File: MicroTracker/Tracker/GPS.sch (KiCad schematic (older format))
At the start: 2 parts, among them U2 TESEO-LIV3F, U3 GP.1575.15.4.B.02

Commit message: started working on gps
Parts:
- removed U2: TESEO-LIV3F, LCC18_9P7X10P1_STM, symbol MicroTracker:TESEO-LIV3F
- removed U3: GP.1575.15.4.B.02, GP.1575.15.4.B.02_TAL, symbol MicroTracker:GP.1575.15.4.B.02
- added BT?: Battery_Cell, symbol Device:Battery_Cell
- added C?: 120pF, symbol Device:C
- added C?: 120p, symbol Device:C
- added C?: 56p, symbol Device:C
- added C?: 1u, symbol Device:C
- added C?: 2.2u, symbol Device:C
- added C?: 100p, symbol Device:C
- added C?: 100n, symbol Device:C
- added C?: 1n, symbol Device:C
- added D?: D_TVS_ALT, symbol Device:D_TVS_ALT
- added F?: B4327, symbol local-symbols:B4327
- added L?: 6.8n, symbol Device:L
- added L?: 56n, symbol Device:L
- added R? (x4): 0, symbol Device:R
- added R?: R, symbol Device:R
- added R?: 100k, symbol Device:R
- added R?: 10k, symbol Device:R
- added U?: TESEO-LIV3F, symbol local-symbols:TESEO-LIV3F
- added U?: BGA725L6, symbol local-symbols:BGA725L6
- added U?: GP.1575.15.4.B.02, GP.1575.15.4.B.02_TAL, symbol MicroTracker:GP.1575.15.4.B.02
- added U?: TPS22943, symbol local-symbols:TPS22943
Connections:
- net labels added: +3.3V, +BATT, ANT_OFF, RF_IN, VCC_RF
- wire segments 5 -> 75
- no-connect marks 2 -> 0
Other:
- note removed: "GPS\n"

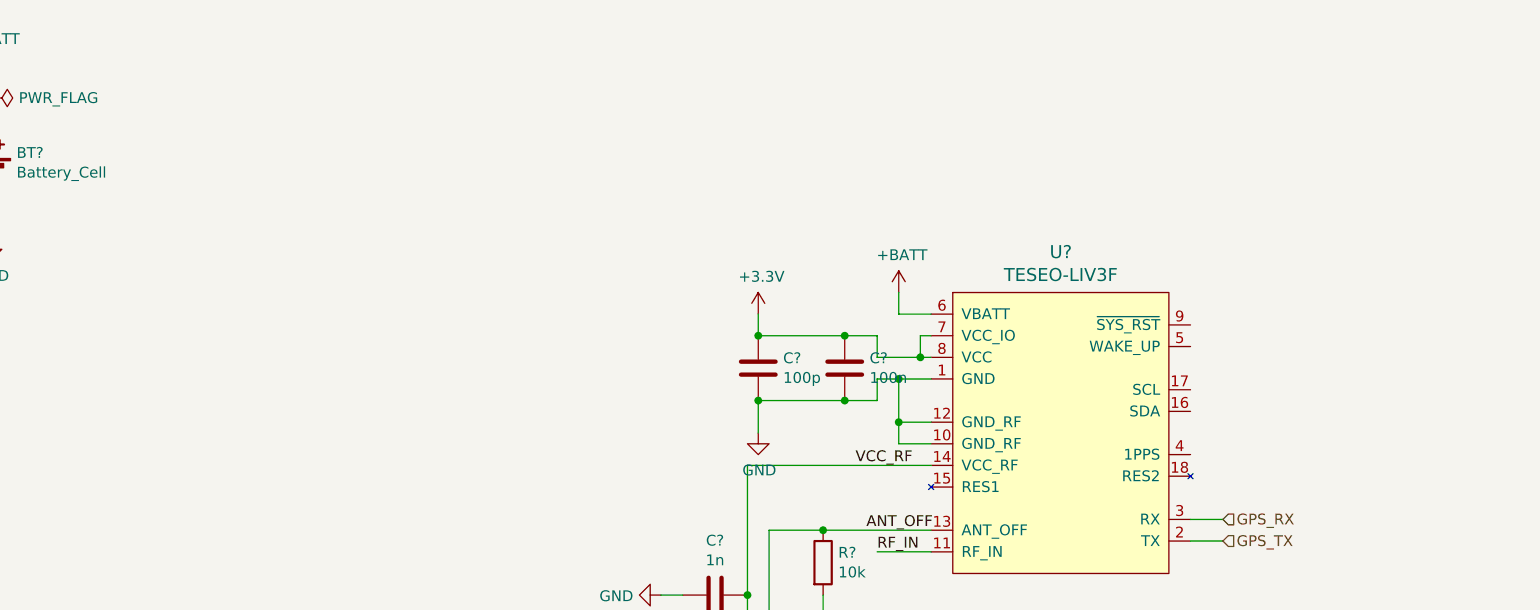
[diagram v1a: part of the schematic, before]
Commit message: gps finished
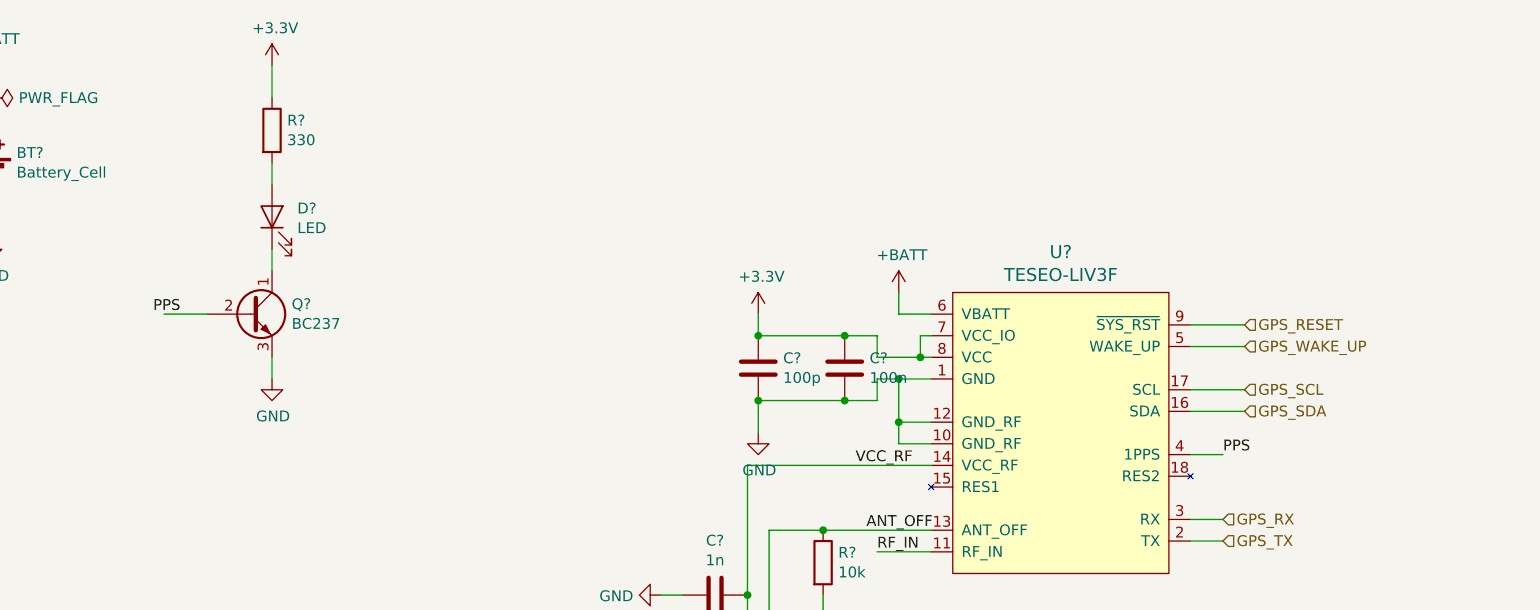
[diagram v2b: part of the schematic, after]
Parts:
- added D?: LED, symbol Device:LED
- added Q?: BC237, Package_TO_SOT_THT:TO-92_Inline, symbol Transistor_BJT:BC237
- added R?: 330, symbol Device:R
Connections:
- net +3V3: now also R?.1
- net GND: now also Q?.3 (E)
- net GPS_SDA: now reaches U?.16 (SDA)
- net GPS_SCL: now reaches U?.17 (SCL)
- net PPS: now reaches U?.4 (1PPS)
- net GPS_WAKE_UP: now reaches U?.5 (WAKE_UP)
- net GPS_RESET: now reaches U?.9 (~SYS_RST)
- new net: D?.2 (A), R?.2
- new net: D?.1 (K), Q?.1 (C)
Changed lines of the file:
@@
 Wire Wire Line
 	4800 3500 4900 3500
+Text Label 7400 2850 0    50   ~ 0
+PPS
+Wire Wire Line
+	7250 2850 7400 2850
+$Comp
+L power:+3.3V #PWR?
+U 1 1 5F0DD0CB
+P 3000 1050
+F 0 "#PWR?" H 3000 900 50  0001 C CNN
+F 1 "+3.3V" H 3015 1223 50  0000 C CNN
+F 2 "" H 3000 1050 50  0001 C CNN
+F 3 "" H 3000 1050 50  0001 C CNN
+	1    3000 1050
+	1    0    0    -1
+$EndComp
+$Comp
+L Device:R R?
+U 1 1 5F0DDA09
+P 3000 1350
+F 0 "R?" H 3070 1396 50  0000 L CNN
+F 1 "330" H 3070 1305 50  0000 L CNN
+F 2 "" V 2930 1350 50  0001 C CNN
+F 3 "~" H 3000 1350 50  0001 C CNN
+	1    3000 1350
+	1    0    0    -1
+$EndComp
+$Comp
+L Device:LED D?
+U 1 1 5F0DE437
+P 3000 1750
+F 0 "D?" V 3039 1633 50  0000 R CNN
+F 1 "LED" V 2948 1633 50  0000 R CNN
+F 2 "" H 3000 1750 50  0001 C CNN
+F 3 "~" H 3000 1750 50  0001 C CNN
+	1    3000 1750
+	0    -1   -1   0
+$EndComp
+$Comp
+L power:GND #PWR?
+U 1 1 5F0DF596
+P 3000 2500
+F 0 "#PWR?" H 3000 2250 50  0001 C CNN
+F 1 "GND" H 3005 2327 50  0000 C CNN
+F 2 "" H 3000 2500 50  0001 C CNN
+F 3 "" H 3000 2500 50  0001 C CNN
+	1    3000 2500
+	1    0    0    -1
+$EndComp
+Wire Wire Line
+	3000 1050 3000 1200
+Wire Wire Line
+	3000 1500 3000 1600
+$Comp
+L Transistor_BJT:BC237 Q?
+U 1 1 5F0E52E0
+P 2900 2200
+F 0 "Q?" H 3091 2246 50  0000 L CNN
+F 1 "BC237" H 3091 2155 50  0000 L CNN
+F 2 "Package_TO_SOT_THT:TO-92_Inline" H 3100 2125 50  0001 L CIN
+F 3 "http://www.onsemi.com/pub_link/Collateral/BC237-D.PDF" H 2900 2200 50  0001 L CNN
+	1    2900 2200
+	1    0    0    -1
+$EndComp
+Text Label 2450 2200 0    50   ~ 0
+PPS
+Wire Wire Line
+	3000 1900 3000 2000
+Wire Wire Line
+	2500 2200 2700 2200
+Wire Wire Line
+	3000 2400 3000 2500
+Text HLabel 7500 2250 2    50   Input ~ 0
+GPS_RESET
+Text HLabel 7500 2350 2    50   Input ~ 0
+GPS_WAKE_UP
+Text HLabel 7500 2550 2    50   Input ~ 0
+GPS_SCL
+Text HLabel 7500 2650 2    50   Input ~ 0
+GPS_SDA
+Wire Wire Line
+	7250 2250 7500 2250
+Wire Wire Line
+	7250 2350 7500 2350
+Wire Wire Line
+	7250 2550 7500 2550
+Wire Wire Line
+	7250 2650 7500 2650
 $EndSCHEMATC

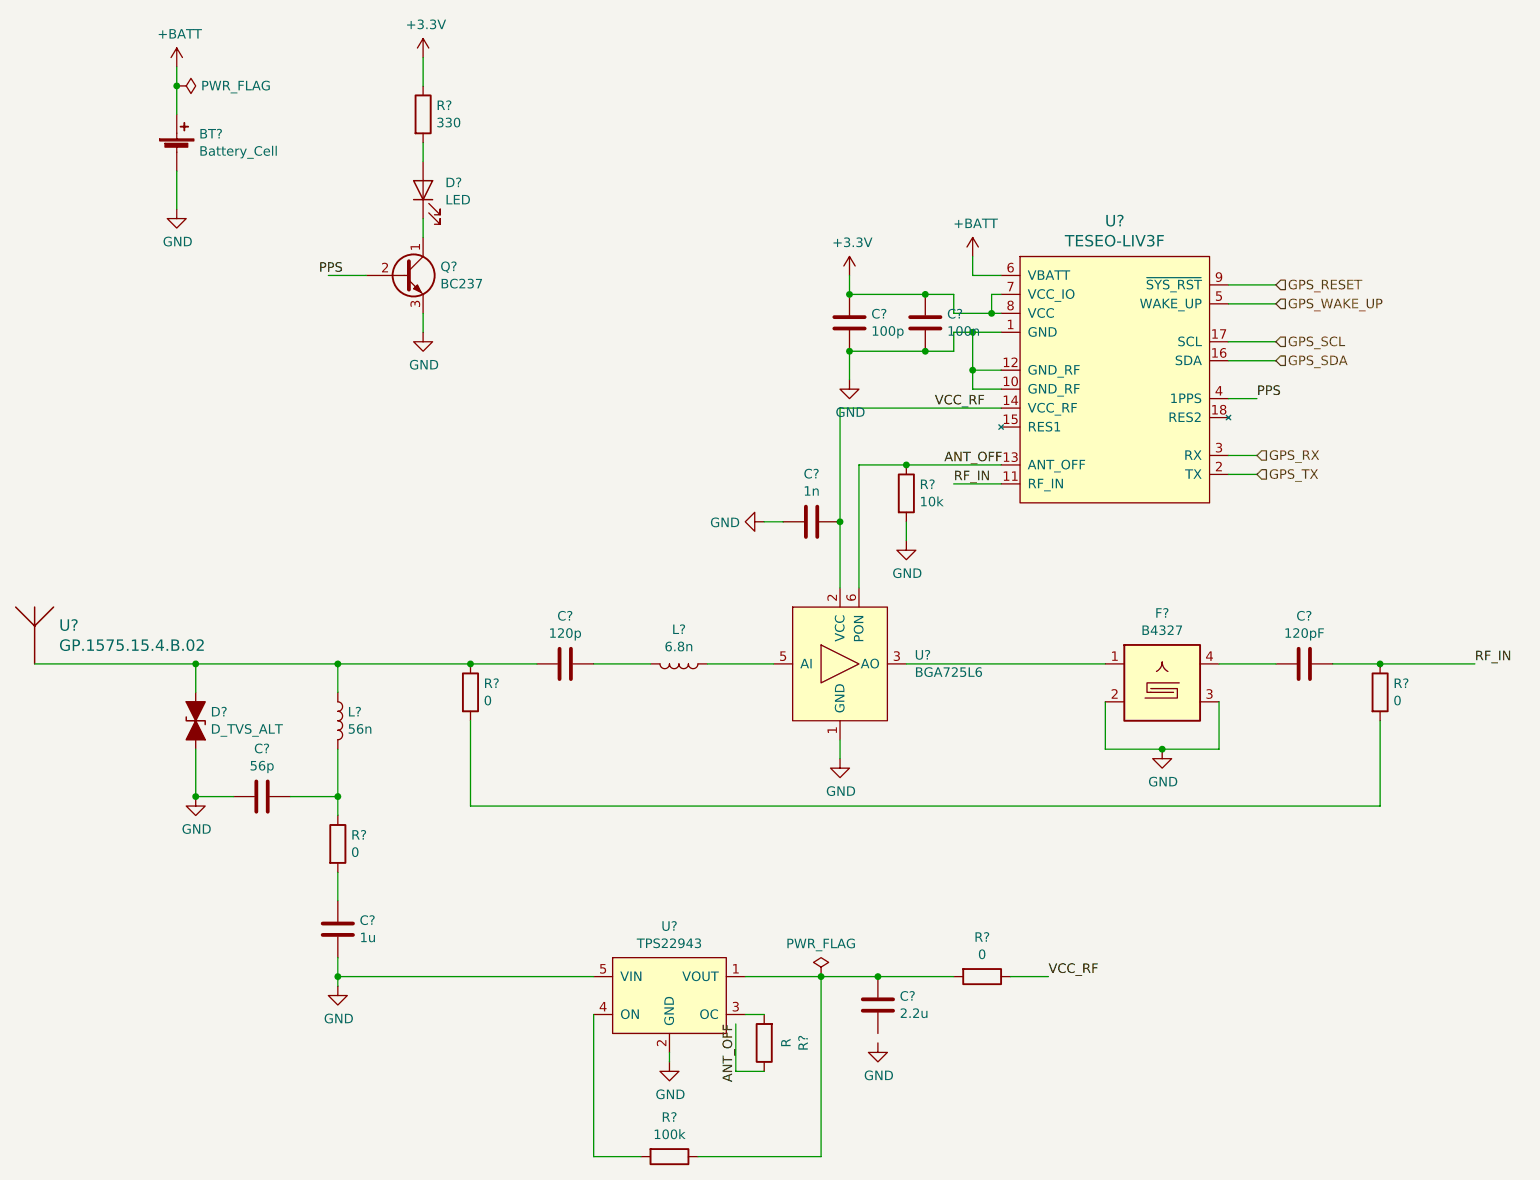
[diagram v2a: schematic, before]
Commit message: added charges
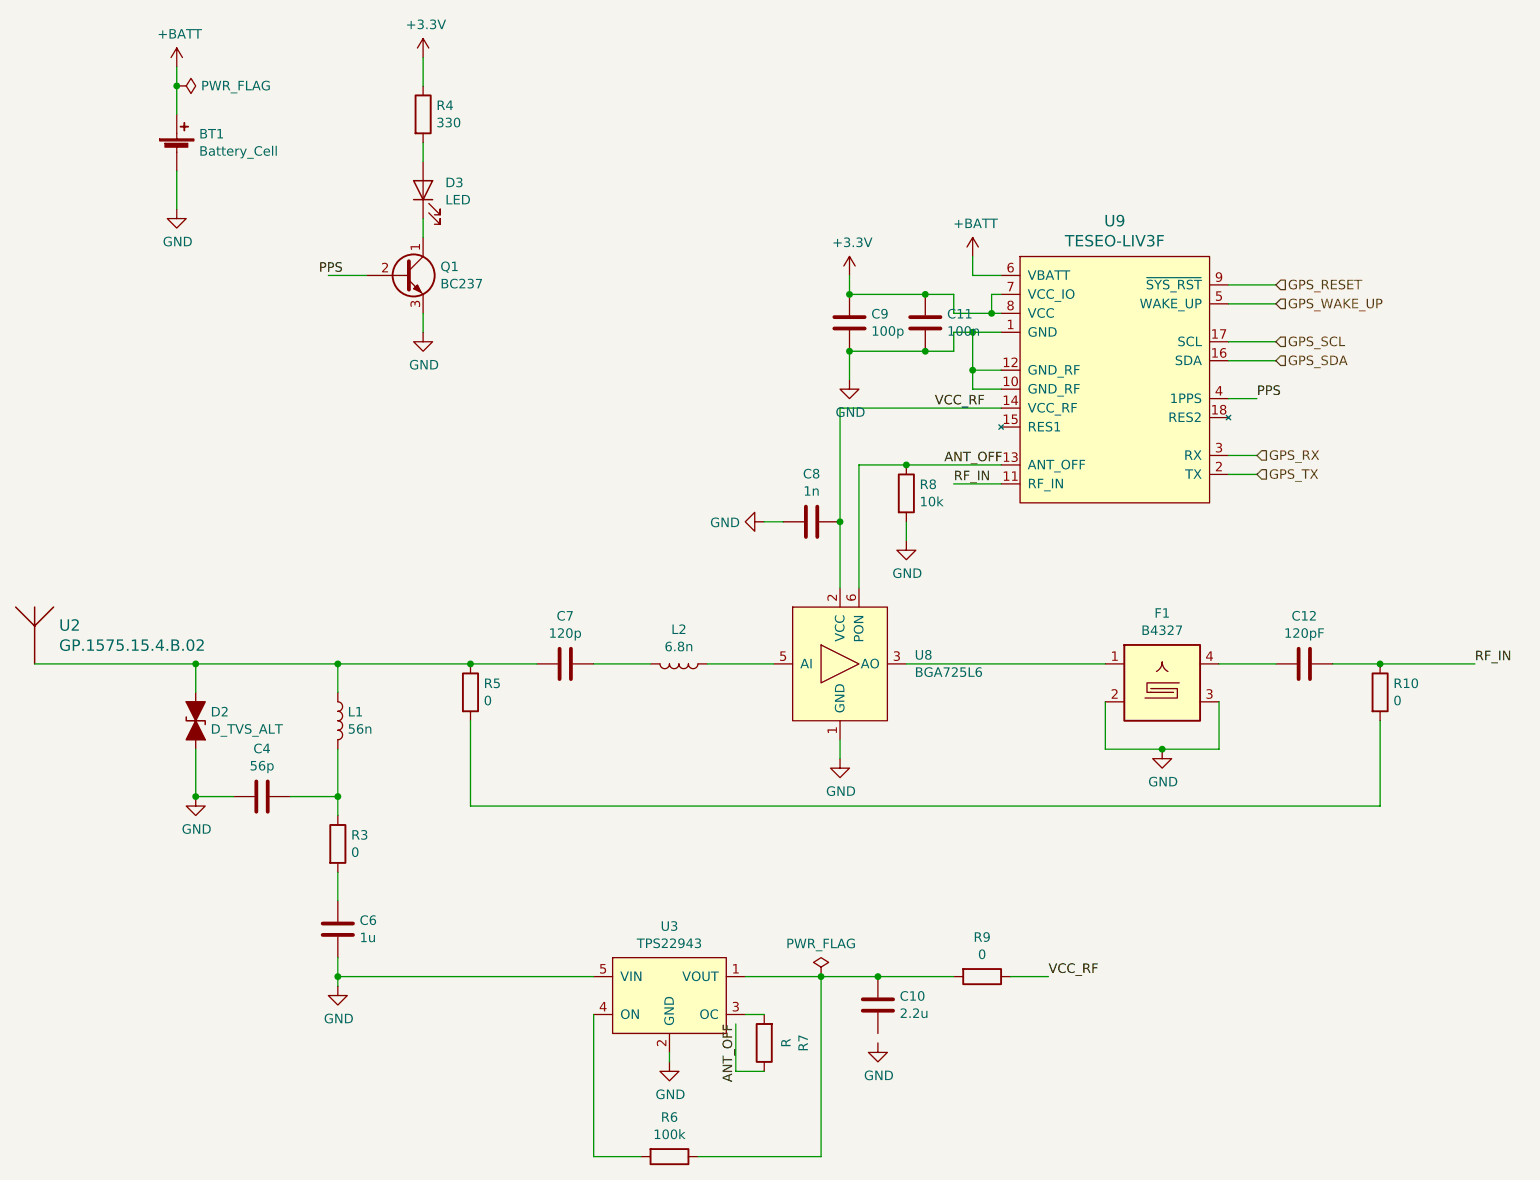
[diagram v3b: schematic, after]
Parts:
- gave numbers to parts that had none: 27

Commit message: assigned parts
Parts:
- BT1: footprint (none) -> local-footprints:Keystone_3030_1x10mm-CoinCell
- C10, C11, C12, C4, C6, C7, C8, C9: footprint (none) -> Capacitor_SMD:C_0805_2012Metric_Pad1.15x1.40mm_HandSolder
- D3: footprint (none) -> LED_SMD:LED_0805_2012Metric_Pad1.15x1.40mm_HandSolder
- F1: footprint (none) -> local-footprints:Filter_1411-5_1.4x1.1mm
- L1, L2: footprint (none) -> Inductor_SMD:L_0805_2012Metric_Pad1.15x1.40mm_HandSolder
- R10, R3, R4, R5, R6, R7, R8, R9: footprint (none) -> Resistor_SMD:R_0805_2012Metric_Pad1.15x1.40mm_HandSolder
- U8: footprint (none) -> local-footprints:TSNP-6_0.8x0.7mm_P0.4mm
- U9: footprint (none) -> local-footprints:TESEO_LIV3F_SMD
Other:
- moved on the sheet: U2
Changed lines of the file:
@@
 F 0 "U9" H 6650 3587 60  0000 C CNN
 F 1 "TESEO-LIV3F" H 6650 3481 60  0000 C CNN
-F 2 "" H 6700 3500 60  0001 L CNN
+F 2 "local-footprints:TESEO_LIV3F_SMD" H 6700 3500 60  0001 L CNN
 F 3 "http://update.maestro-wireless.com/GNSS/A2235-H/Maestro_A2135_HA2235_H_v11.pdf" H 6700 3600 60  0001 L CNN
 F 4 "497-18163-ND" H 6700 3700 60  0001 L CNN "Digi-Key_PN"
@@
 F 0 "U8" H 5594 4296 50  0000 L CNN
 F 1 "BGA725L6" H 5594 4205 50  0000 L CNN
-F 2 "" H 4850 4500 50  0001 C CNN
+F 2 "local-footprints:TSNP-6_0.8x0.7mm_P0.4mm" H 4850 4500 50  0001 C CNN
 F 3 "https://www.infineon.com/dgdl/BGA725L6_V2+0.pdf?folderId=db3a30431f848401011fcbf2ab4c04c4&fileId=db3a30433784a0400137ef9a4d341f23" H 5500 4600 50  0001 L CNN
 F 4 "Active" H 5500 4700 50  0001 L CNN "Status"
@@
 F 0 "F1" H 6900 4717 50  0000 C CNN
 F 1 "B4327" H 6900 4626 50  0000 C CNN
-F 2 "" H 6900 4000 50  0001 C CNN
+F 2 "local-footprints:Filter_1411-5_1.4x1.1mm" H 6900 4000 50  0001 C CNN
 F 3 "https://product.tdk.com/search-template/en/documents/data_sheet/40/ds/mc/B9482.pdf" H 7000 4950 50  0001 L CNN
 F 4 "Active" H 7000 4850 50  0001 L CNN "Status"
@@
 F 0 "C12" V 7398 4250 50  0000 C CNN
 F 1 "120pF" V 7489 4250 50  0000 C CNN
-F 2 "" H 7688 4100 50  0001 C CNN
+F 2 "Capacitor_SMD:C_0805_2012Metric_Pad1.15x1.40mm_HandSolder" H 7688 4100 50  0001 C CNN
 F 3 "~" H 7650 4250 50  0001 C CNN
 	1    7650 4250
@@
 F 0 "L2" V 4169 4250 50  0000 C CNN
 F 1 "6.8n" V 4260 4250 50  0000 C CNN
-F 2 "" H 4350 4250 50  0001 C CNN
+F 2 "Inductor_SMD:L_0805_2012Metric_Pad1.15x1.40mm_HandSolder" H 4350 4250 50  0001 C CNN
 F 3 "~" H 4350 4250 50  0001 C CNN
 	1    4350 4250
@@
 F 0 "C7" V 3498 4250 50  0000 C CNN
 F 1 "120p" V 3589 4250 50  0000 C CNN
-F 2 "" H 3788 4100 50  0001 C CNN
+F 2 "Capacitor_SMD:C_0805_2012Metric_Pad1.15x1.40mm_HandSolder" H 3788 4100 50  0001 C CNN
 F 3 "~" H 3750 4250 50  0001 C CNN
 	1    3750 4250
@@
 F 0 "R5" H 3320 4446 50  0000 L CNN
 F 1 "0" H 3320 4355 50  0000 L CNN
-F 2 "" V 3180 4400 50  0001 C CNN
+F 2 "Resistor_SMD:R_0805_2012Metric_Pad1.15x1.40mm_HandSolder" V 3180 4400 50  0001 C CNN
 F 3 "~" H 3250 4400 50  0001 C CNN
 	1    3250 4400
@@
 F 0 "R10" H 8120 4446 50  0000 L CNN
 F 1 "0" H 8120 4355 50  0000 L CNN
-F 2 "" V 7980 4400 50  0001 C CNN
+F 2 "Resistor_SMD:R_0805_2012Metric_Pad1.15x1.40mm_HandSolder" V 7980 4400 50  0001 C CNN
 F 3 "~" H 8050 4400 50  0001 C CNN
 	1    8050 4400
@@
 F 0 "L1" H 2602 4596 50  0000 L CNN
 F 1 "56n" H 2602 4505 50  0000 L CNN
-F 2 "" H 2550 4550 50  0001 C CNN
+F 2 "Inductor_SMD:L_0805_2012Metric_Pad1.15x1.40mm_HandSolder" H 2550 4550 50  0001 C CNN
 F 3 "~" H 2550 4550 50  0001 C CNN
 	1    2550 4550
@@
 L MicroTracker:GP.1575.15.4.B.02 U2
 U 1 1 5F07D482
-P 1050 4250
-F 0 "U2" H 1079 4453 60  0000 L CNN
-F 1 "GP.1575.15.4.B.02" H 1079 4347 60  0000 L CNN
-F 2 "GP.1575.15.4.B.02_TAL" H 1725 3040 60  0001 C CNN
-F 3 "" H 1050 4250 60  0000 C CNN
-	1    1050 4250
+P 1050 4200
+F 0 "U2" H 1079 4403 60  0000 L CNN
+F 1 "GP.1575.15.4.B.02" H 1079 4297 60  0000 L CNN
+F 2 "GP.1575.15.4.B.02_TAL" H 1725 2990 60  0001 C CNN
+F 3 "" H 1050 4200 60  0000 C CNN
+	1    1050 4200
 	1    0    0    -1
 $EndComp
@@
 F 0 "C4" V 1898 4950 50  0000 C CNN
 F 1 "56p" V 1989 4950 50  0000 C CNN
-F 2 "" H 2188 4800 50  0001 C CNN
+F 2 "Capacitor_SMD:C_0805_2012Metric_Pad1.15x1.40mm_HandSolder" H 2188 4800 50  0001 C CNN
 F 3 "~" H 2150 4950 50  0001 C CNN
 	1    2150 4950
@@
 F 0 "R3" H 2620 5246 50  0000 L CNN
 F 1 "0" H 2620 5155 50  0000 L CNN
-F 2 "" V 2480 5200 50  0001 C CNN
+F 2 "Resistor_SMD:R_0805_2012Metric_Pad1.15x1.40mm_HandSolder" V 2480 5200 50  0001 C CNN
 F 3 "~" H 2550 5200 50  0001 C CNN
 	1    2550 5200
@@
 F 0 "C6" H 2665 5696 50  0000 L CNN
 F 1 "1u" H 2665 5605 50  0000 L CNN
-F 2 "" H 2588 5500 50  0001 C CNN
+F 2 "Capacitor_SMD:C_0805_2012Metric_Pad1.15x1.40mm_HandSolder" H 2588 5500 50  0001 C CNN
 F 3 "~" H 2550 5650 50  0001 C CNN
 	1    2550 5650
@@
 F 0 "R7" V 4593 6250 50  0000 C CNN
 F 1 "R" V 4684 6250 50  0000 C CNN
-F 2 "" V 4730 6250 50  0001 C CNN
+F 2 "Resistor_SMD:R_0805_2012Metric_Pad1.15x1.40mm_HandSolder" V 4730 6250 50  0001 C CNN
 F 3 "~" H 4800 6250 50  0001 C CNN
 	1    4800 6250
@@
 F 0 "C10" H 5515 6096 50  0000 L CNN
 F 1 "2.2u" H 5515 6005 50  0000 L CNN
-F 2 "" H 5438 5900 50  0001 C CNN
+F 2 "Capacitor_SMD:C_0805_2012Metric_Pad1.15x1.40mm_HandSolder" H 5438 5900 50  0001 C CNN
 F 3 "~" H 5400 6050 50  0001 C CNN
 	1    5400 6050
@@
 F 0 "R9" V 5743 5900 50  0000 C CNN
 F 1 "0" V 5834 5900 50  0000 C CNN
-F 2 "" V 5880 5900 50  0001 C CNN
+F 2 "Resistor_SMD:R_0805_2012Metric_Pad1.15x1.40mm_HandSolder" V 5880 5900 50  0001 C CNN
 F 3 "~" H 5950 5900 50  0001 C CNN
 	1    5950 5900
@@
 F 0 "R6" V 4093 6850 50  0000 C CNN
 F 1 "100k" V 4184 6850 50  0000 C CNN
-F 2 "" V 4230 6850 50  0001 C CNN
+F 2 "Resistor_SMD:R_0805_2012Metric_Pad1.15x1.40mm_HandSolder" V 4230 6850 50  0001 C CNN
 F 3 "~" H 4300 6850 50  0001 C CNN
 	1    4300 6850
@@
 F 0 "BT1" H 1818 1646 50  0000 L CNN
 F 1 "Battery_Cell" H 1818 1555 50  0000 L CNN
-F 2 "" V 1700 1610 50  0001 C CNN
+F 2 "local-footprints:Keystone_3030_1x10mm-CoinCell" V 1700 1610 50  0001 C CNN
 F 3 "~" V 1700 1610 50  0001 C CNN
 	1    1700 1550
@@
 F 0 "C9" H 5365 2496 50  0000 L CNN
 F 1 "100p" H 5365 2405 50  0000 L CNN
-F 2 "" H 5288 2300 50  0001 C CNN
+F 2 "Capacitor_SMD:C_0805_2012Metric_Pad1.15x1.40mm_HandSolder" H 5288 2300 50  0001 C CNN
 F 3 "~" H 5250 2450 50  0001 C CNN
 	1    5250 2450
@@
 F 0 "C11" H 5765 2496 50  0000 L CNN
 F 1 "100n" H 5765 2405 50  0000 L CNN
-F 2 "" H 5688 2300 50  0001 C CNN
+F 2 "Capacitor_SMD:C_0805_2012Metric_Pad1.15x1.40mm_HandSolder" H 5688 2300 50  0001 C CNN
 F 3 "~" H 5650 2450 50  0001 C CNN
 	1    5650 2450
@@
 F 0 "R8" H 5620 3396 50  0000 L CNN
 F 1 "10k" H 5620 3305 50  0000 L CNN
-F 2 "" V 5480 3350 50  0001 C CNN
+F 2 "Resistor_SMD:R_0805_2012Metric_Pad1.15x1.40mm_HandSolder" V 5480 3350 50  0001 C CNN
 F 3 "~" H 5550 3350 50  0001 C CNN
 	1    5550 3350
@@
 F 0 "C8" V 4798 3500 50  0000 C CNN
 F 1 "1n" V 4889 3500 50  0000 C CNN
-F 2 "" H 5088 3350 50  0001 C CNN
+F 2 "Capacitor_SMD:C_0805_2012Metric_Pad1.15x1.40mm_HandSolder" H 5088 3350 50  0001 C CNN
 F 3 "~" H 5050 3500 50  0001 C CNN
 	1    5050 3500
@@
 F 0 "R4" H 3070 1396 50  0000 L CNN
 F 1 "330" H 3070 1305 50  0000 L CNN
-F 2 "" V 2930 1350 50  0001 C CNN
+F 2 "Resistor_SMD:R_0805_2012Metric_Pad1.15x1.40mm_HandSolder" V 2930 1350 50  0001 C CNN
 F 3 "~" H 3000 1350 50  0001 C CNN
 	1    3000 1350
@@
 F 0 "D3" V 3039 1633 50  0000 R CNN
 F 1 "LED" V 2948 1633 50  0000 R CNN
-F 2 "" H 3000 1750 50  0001 C CNN
+F 2 "LED_SMD:LED_0805_2012Metric_Pad1.15x1.40mm_HandSolder" H 3000 1750 50  0001 C CNN
 F 3 "~" H 3000 1750 50  0001 C CNN
 	1    3000 1750
@@
 Wire Wire Line
 	7250 2650 7500 2650
+Wire Wire Line
+	950  4200 950  4250
 $EndSCHEMATC
